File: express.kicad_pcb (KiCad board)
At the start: 4 copper layers, 180 x 35 mm, 180 parts, among them J1001 SJ2-25504B-SMT-TR, J101 Cortex_Debug, J102 JAE_DX07S016JA3, J1101 SJ2-25504B-SMT-TR, J1201 SJ2-25504B-SMT-TR, J1301 SJ2-25504B-SMT-TR, J1401 SJ2-25504B-SMT-TR, J1501 SJ2-25504B-SMT-TR, J1601 SJ2-25504B-SMT-TR, J1701 SJ2-25504B-SMT-TR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

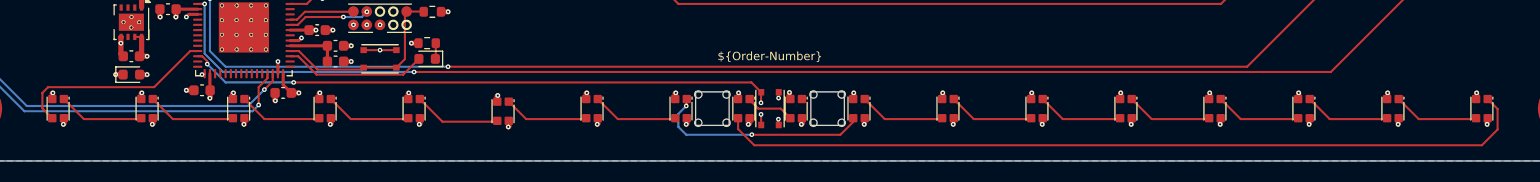
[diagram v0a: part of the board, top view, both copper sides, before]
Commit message: Fix LED location
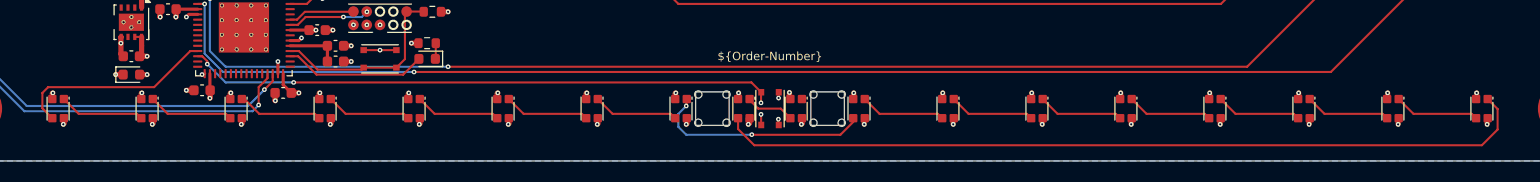
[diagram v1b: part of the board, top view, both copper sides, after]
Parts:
- INFO101: value ORDER-NUMBER -> Order_Number
- U101: value TPS78433QWDRBRQ1 -> TPS78433QWDRBRQ1
- moved D501 0.25 mm to (101.5, 114.8)
- moved D801 0.25 mm to (127.0, 114.8)

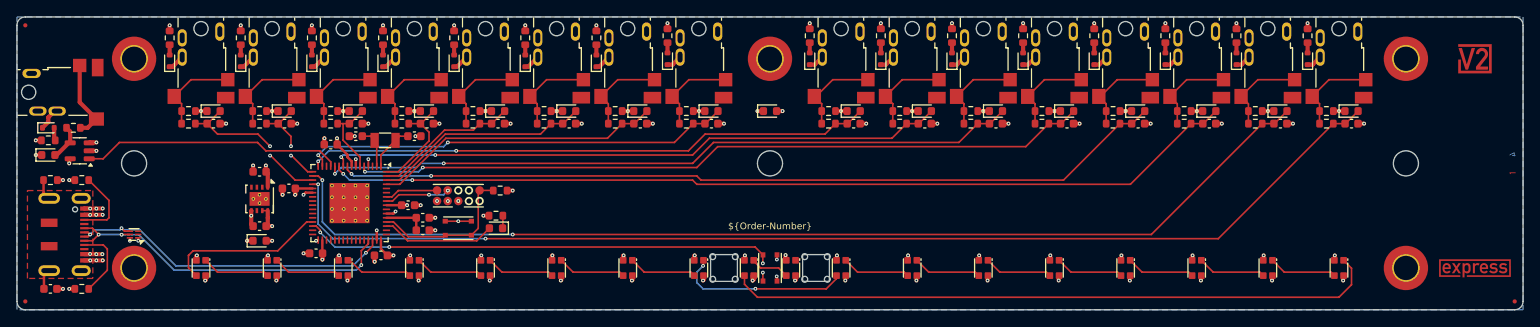
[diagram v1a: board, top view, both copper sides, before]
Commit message: Replace TRS sockets
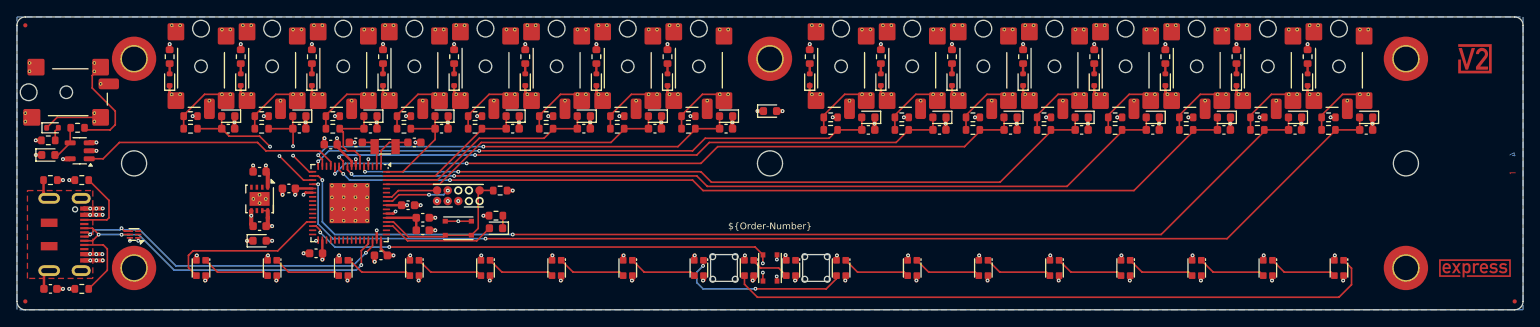
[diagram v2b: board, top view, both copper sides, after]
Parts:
- J1001, J1101, J1201, J1301, J1401, J1501, J1601, J1701, J1801, J201, J301, J401, J501, J601, J701, J801, J901: value SJ2-25504B-SMT-TR -> SJ2-25404B-SMT-TR; footprint V2_Connector_Audio:CUI_SJ2-25504B-SMT-TR -> V2_Connector_Audio:CUI_SJ2-25404B-SMT-TR
- moved D1002 2.50 mm to (140.2, 92.2)
- moved D1101 2.50 mm to (157.2, 92.2)
- moved D1201 2.50 mm to (165.8, 92.2)
- moved D1301 2.50 mm to (174.2, 92.2)
- moved D1401 2.50 mm to (182.8, 92.2)
- moved D1501 2.50 mm to (191.2, 92.2)
- moved D1601 2.50 mm to (199.8, 92.2)
- moved D1701 2.50 mm to (208.2, 92.2)
- moved D1801 2.50 mm to (216.8, 92.2)
- moved R1001 2.50 mm to (140.2, 89.5)
- moved R1101 2.50 mm to (157.2, 89.5)
- moved R1201 2.50 mm to (165.8, 89.5)
- moved R1301 2.50 mm to (174.2, 89.5)
- moved R1401 2.50 mm to (182.8, 89.5)
- moved R1501 2.50 mm to (191.2, 89.5)
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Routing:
- net /MIDI Out/Ring: track 2.90 -> 6.97 mm
- net / Expression Input 4/Tip: track 10.8 -> 7.11 mm
- net / Expression Input 3/Tip: track 10.8 -> 7.11 mm
- net / Expression Input 2/Tip: track 10.8 -> 7.11 mm
- net / Expression Input 1/Tip: track 10.8 -> 7.11 mm
- net / Expression Input 8/Tip: track 10.8 -> 7.11 mm
- net / Expression Input 7/Tip: track 10.8 -> 7.11 mm
- net / Expression Input 6/Tip: track 10.8 -> 7.11 mm
- net / Expression Input 5 /Tip: track 10.8 -> 7.22 mm
- net / Expression Input 13/Tip: track 10.8 -> 7.36 mm
- net / Expression Input 10/Tip: track 10.8 -> 7.36 mm
- net / Expression Input 9/Tip: track 10.8 -> 7.36 mm
- net / Expression Input 16/Tip: track 10.8 -> 7.36 mm
- net / Expression Input 15/Tip: track 10.8 -> 7.36 mm
- net / Expression Input 14/Tip: track 10.8 -> 7.36 mm
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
